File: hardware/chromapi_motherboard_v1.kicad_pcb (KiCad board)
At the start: 2 copper layers, 140 parts, among them J1 Battery Input, J10 Conn_FSR_TopLeft, J11 Conn_FSR_TopRight, J12 Conn_FSR_BotLeft, J13 Conn_FSR_BotRight, J14 RPI_Connector, J2 Power Switch, J3 USB_C_Receptacle_USB2.0_14P, J4 Conn_ST_STDC14, J5 Conn_TopLeft, J6 Conn_TopRight, J7 Conn_BotLeft, J8 Conn_BotRight, J9 Speaker connector, M1 Noctua NF-A4x10, Q1 PSMN1R5-30YL, Q2 PSMN1R5-30YL, Q3 AO4435, Q4 AO4468, U1 HY2120, U2 CN3302, U3 TPS568230, U4 LD39050PU33R, U5 74AHCT125, U6 STM32G431KBTx, U7 SN74LVC1T45DBV, U8 MAX98357A, U9 BNO055, Y1 32.768k

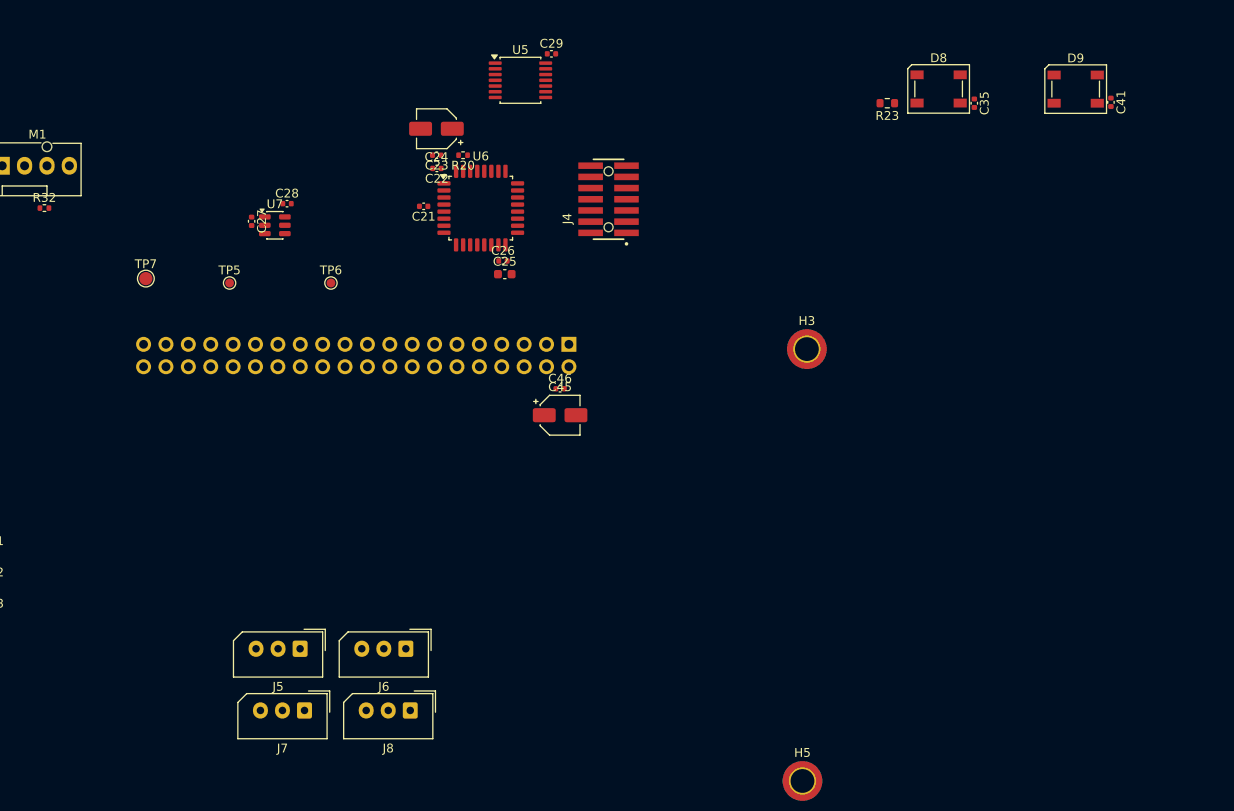
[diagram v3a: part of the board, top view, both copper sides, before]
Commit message: Adding some MPN/MPR
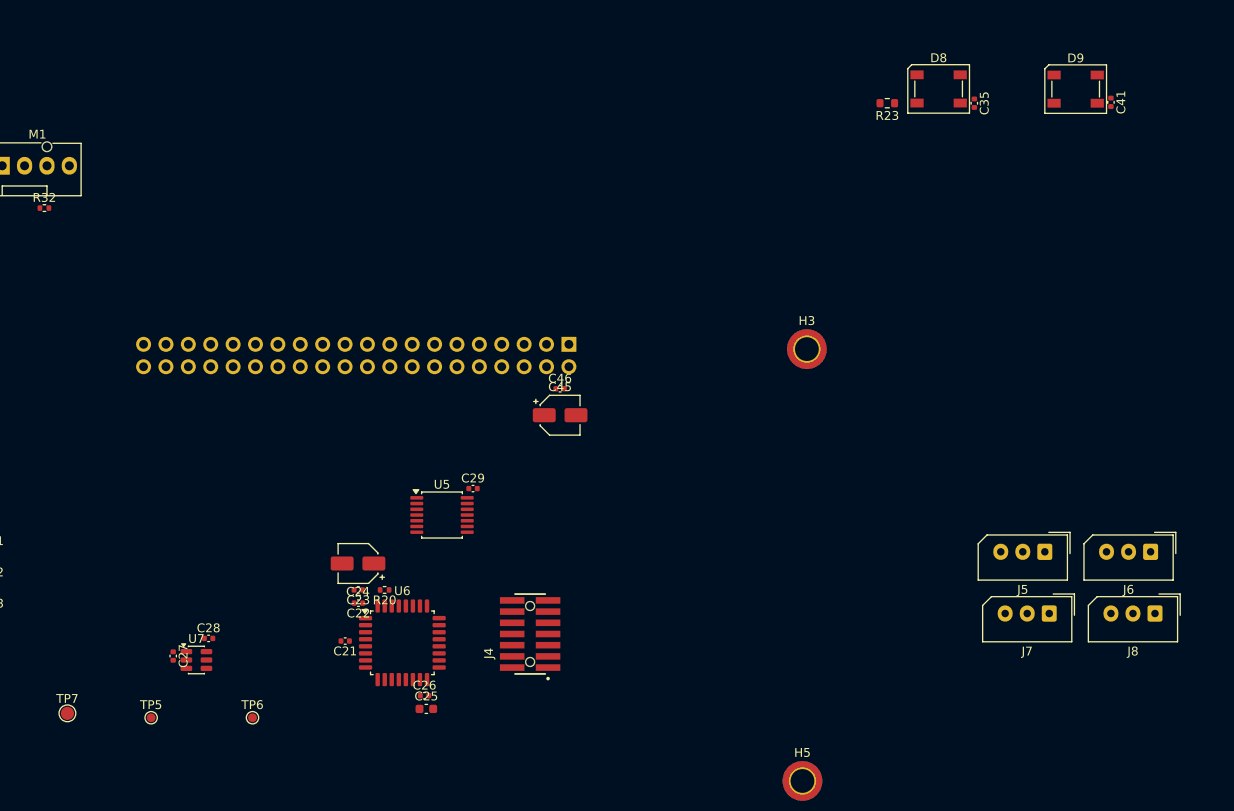
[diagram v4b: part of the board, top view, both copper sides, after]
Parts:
- moved J5 85.2 mm to (208.0, 73.5)
- moved J6 85.2 mm to (220.0, 73.5)
- moved J7 85.2 mm to (208.5, 80.5)
- moved J8 85.2 mm to (220.5, 80.5)
- moved C21 50.1 mm to (128.6, 83.6)
- moved C22 50.1 mm to (130.1, 79.3)
- moved C23 50.1 mm to (130.1, 77.8)
- moved C24 50.1 mm to (130.1, 74.8)
- moved C25 50.1 mm to (137.8, 91.3)
- moved C26 50.1 mm to (137.6, 89.8)
- moved C27 50.1 mm to (109.1, 85.3)
- moved C28 50.1 mm to (113.1, 83.3)
- moved C29 50.1 mm to (143.1, 66.3)
- moved J4 50.1 mm to (149.6, 82.8)
- moved R20 50.1 mm to (133.1, 77.8)
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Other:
- copper layers 2 -> 4
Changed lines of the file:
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@@
 	)
 	(layers
-		(0 "F.Cu" signal)
-		(2 "B.Cu" signal)
+		(0 "F.Cu" signal "F.Cu-SIGNAL")
+		(4 "In1.Cu" signal "In1.Cu-GND")
+		(6 "In2.Cu" signal "In2.Cu-PWR")
+		(2 "B.Cu" signal "B.Cu-SIGNAL")
 		(9 "F.Adhes" user "F.Adhesive")
 		(11 "B.Adhes" user "B.Adhesive")
@@
 	)
 	(setup
+		(stackup
+			(layer "F.SilkS"
+				(type "Top Silk Screen")
+			)
+			(layer "F.Paste"
+				(type "Top Solder Paste")
+			)
+			(layer "F.Mask"
+				(type "Top Solder Mask")
+				(thickness 0.01)
+			)
+			(layer "F.Cu"
+				(type "copper")
+				(thickness 0.035)
+			)
+			(layer "dielectric 1"
+				(type "prepreg")
+				(thickness 0.1)
+				(material "FR4")
+				(epsilon_r 4.5)
+				(loss_tangent 0.02)
+			)
+			(layer "In1.Cu"
+				(type "copper")
+				(thickness 0.035)
+			)
+			(layer "dielectric 2"
+				(type "core")
+				(thickness 1.24)
+				(material "FR4")
+				(epsilon_r 4.5)
+				(loss_tangent 0.02)
+			)
+			(layer "In2.Cu"
+				(type "copper")
+				(thickness 0.035)
+			)
+			(layer "dielectric 3"
+				(type "prepreg")
+				(thickness 0.1)
+				(material "FR4")
+				(epsilon_r 4.5)
+				(loss_tangent 0.02)
+			)
+			(layer "B.Cu"
+				(type "copper")
+				(thickness 0.035)
+			)
+			(layer "B.Mask"
+				(type "Bottom Solder Mask")
+				(thickness 0.01)
+			)
+			(layer "B.Paste"
+				(type "Bottom Solder Paste")
+			)
+			(layer "B.SilkS"
+				(type "Bottom Silk Screen")
+			)
+			(copper_finish "None")
+			(dielectric_constraints no)
+		)
 		(pad_to_mask_clearance 0)
+		(pad_to_paste_clearance_ratio -0.1)
 		(allow_soldermask_bridges_in_footprints no)
 		(tenting front back)
@@
 	(footprint "Capacitor_SMD:C_0402_1005Metric"
 		(layer "F.Cu")
-		(at 139 28.5 180)
+		(at 130.1 77.825 180)
 		(descr "Capacitor SMD 0402 (1005 Metric), square (rectangular) end terminal, IPC-7351 nominal, (Body size source: IPC-SM-782 page 76, https://www.pcb-3d.com/wordpress/wp-content/uploads/ipc-sm-782a_amendment_1_and_2.pdf), generated with kicad-footprint-generator")
 		(tags "capacitor")
@@
 	(footprint "Capacitor_SMD:C_0402_1005Metric"
 		(layer "F.Cu")
-		(at 146.52 40.5)
+		(at 137.62 89.825)
 		(descr "Capacitor SMD 0402 (1005 Metric), square (rectangular) end terminal, IPC-7351 nominal, (Body size source: IPC-SM-782 page 76, https://www.pcb-3d.com/wordpress/wp-content/uploads/ipc-sm-782a_amendment_1_and_2.pdf), generated with kicad-footprint-generator")
 		(tags "capacitor")
@@
 	(footprint "Package_QFP:LQFP-32_7x7mm_P0.8mm"
 		(layer "F.Cu")
-		(at 144 34.5)
+		(at 135.1 83.825)
 		(descr "LQFP, 32 Pin (https://www.nxp.com/docs/en/package-information/SOT358-1.pdf), generated with kicad-footprint-generator ipc_gullwing_generator.py")
 		(tags "LQFP QFP")
@@
 	(footprint "Capacitor_SMD:C_0402_1005Metric"
 		(layer "F.Cu")
-		(at 139.02 30 180)
+		(at 130.12 79.325 180)
 		(descr "Capacitor SMD 0402 (1005 Metric), square (rectangular) end terminal, IPC-7351 nominal, (Body size source: IPC-SM-782 page 76, https://www.pcb-3d.com/wordpress/wp-content/uploads/ipc-sm-782a_amendment_1_and_2.pdf), generated with kicad-footprint-generator")
 		(tags "capacitor")
@@
 	(footprint "Connector_Molex:Molex_SPOX_5267-03A_1x03_P2.50mm_Vertical"
 		(layer "F.Cu")
-		(at 123.5 84.5 180)
+		(at 208 73.5 180)
 		(descr "Molex SPOX Connector System, 5267-03A, 3 Pins per row (http://www.molex.com/pdm_docs/sd/022035035_sd.pdf), generated with kicad-footprint-generator")
 		(tags "connector Molex SPOX vertical")
@@
 	(footprint "Package_TO_SOT_SMD:SOT-23-6"
 		(layer "F.Cu")
-		(at 120.6375 36.45)
+		(at 111.7375 85.775)
 		(descr "SOT, 6 Pin (JEDEC MO-178 Var AB https://www.jedec.org/document_search?search_api_views_fulltext=MO-178), generated with kicad-footprint-generator ipc_gullwing_generator.py")
 		(tags "SOT TO_SOT_SMD")
@@
 	(footprint "Connector_Molex:Molex_SPOX_5267-03A_1x03_P2.50mm_Vertical"
 		(layer "F.Cu")
-		(at 136 91.5 180)
+		(at 220.5 80.5 180)
 		(descr "Molex SPOX Connector System, 5267-03A, 3 Pins per row (http://www.molex.com/pdm_docs/sd/022035035_sd.pdf), generated with kicad-footprint-generator")
 		(tags "connector Molex SPOX vertical")
@@
 	(footprint "TestPoint:TestPoint_Pad_D1.0mm"
 		(layer "F.Cu")
-		(at 115.5 43)
+		(at 106.6 92.325)
 		(descr "SMD pad as test Point, diameter 1.0mm")
 		(tags "test point SMD pad")
@@
 	(footprint "Connector_Molex:Molex_SPOX_5267-03A_1x03_P2.50mm_Vertical"
 		(layer "F.Cu")
-		(at 124 91.5 180)
+		(at 208.5 80.5 180)
 		(descr "Molex SPOX Connector System, 5267-03A, 3 Pins per row (http://www.molex.com/pdm_docs/sd/022035035_sd.pdf), generated with kicad-footprint-generator")
 		(tags "connector Molex SPOX vertical")
@@
 	(footprint "Capacitor_SMD:C_0402_1005Metric"
 		(layer "F.Cu")
-		(at 122.02 34)
+		(at 113.12 83.325)
 		(descr "Capacitor SMD 0402 (1005 Metric), square (rectangular) end terminal, IPC-7351 nominal, (Body size source: IPC-SM-782 page 76, https://www.pcb-3d.com/wordpress/wp-content/uploads/ipc-sm-782a_amendment_1_and_2.pdf), generated with kicad-footprint-generator")
 		(tags "capacitor")
@@
 	(footprint "Chromapi_FP:SAMTEC_FTSH-107-01-L-DV-K-A"
 		(layer "F.Cu")
-		(at 158.5 33.5 90)
+		(at 149.6 82.825 90)
 		(descr "translated Allegro footprint")
 		(property "Reference" "J4"
@@
 	(footprint "Capacitor_SMD:C_0402_1005Metric"
 		(layer "F.Cu")
-		(at 152.02 17)
+		(at 143.12 66.325)
 		(descr "Capacitor SMD 0402 (1005 Metric), square (rectangular) end terminal, IPC-7351 nominal, (Body size source: IPC-SM-782 page 76, https://www.pcb-3d.com/wordpress/wp-content/uploads/ipc-sm-782a_amendment_1_and_2.pdf), generated with kicad-footprint-generator")
 		(tags "capacitor")
@@
 	(footprint "Capacitor_SMD:C_0402_1005Metric"
 		(layer "F.Cu")
-		(at 137.52 34.3 180)
+		(at 128.62 83.625 180)
 		(descr "Capacitor SMD 0402 (1005 Metric), square (rectangular) end terminal, IPC-7351 nominal, (Body size source: IPC-SM-782 page 76, https://www.pcb-3d.com/wordpress/wp-content/uploads/ipc-sm-782a_amendment_1_and_2.pdf), generated with kicad-footprint-generator")
 		(tags "capacitor")
@@
 	(footprint "TestPoint:TestPoint_Pad_D1.0mm"
 		(layer "F.Cu")
-		(at 127 43)
+		(at 118.1 92.325)
 		(descr "SMD pad as test Point, diameter 1.0mm")
 		(tags "test point SMD pad")
@@
 	(footprint "Package_SO:TSSOP-14_4.4x5mm_P0.65mm"
 		(layer "F.Cu")
-		(at 148.5 20)
+		(at 139.6 69.325)
 		(descr "TSSOP, 14 Pin (JEDEC MO-153 variation AB-1, 1.00mm body thickness, https://www.jedec.org/document_search?search_api_views_fulltext=MO-153), generated with kicad-footprint-generator ipc_gullwing_generator.py")
 		(tags "TSSOP SO")
@@
 	(footprint "Capacitor_SMD:C_0603_1608Metric"
 		(layer "F.Cu")
-		(at 146.725 42)
+		(at 137.825 91.325)
 		(descr "Capacitor SMD 0603 (1608 Metric), square (rectangular) end terminal, IPC-7351 nominal, (Body size source: IPC-SM-782 page 76, https://www.pcb-3d.com/wordpress/wp-content/uploads/ipc-sm-782a_amendment_1_and_2.pdf), generated with kicad-footprint-generator")
 		(tags "capacitor")
@@
 	(footprint "Capacitor_SMD:CP_Elec_4x4.5"
 		(layer "F.Cu")
-		(at 138.97 25.5 180)
+		(at 130.07 74.825 180)
 		(descr "SMD capacitor, aluminum electrolytic, Nichicon, 4.0x4.5mm")
 		(tags "capacitor electrolytic")
@@
 	(footprint "TestPoint:TestPoint_Pad_D1.5mm"
 		(layer "F.Cu")
-		(at 106 42.5)
+		(at 97.1 91.825)
 		(descr "SMD pad as test Point, diameter 1.5mm")
 		(tags "test point SMD pad")
@@
 	(footprint "Resistor_SMD:R_0402_1005Metric"
 		(layer "F.Cu")
-		(at 141.99 28.5 180)
+		(at 133.09 77.825 180)
 		(descr "Resistor SMD 0402 (1005 Metric), square (rectangular) end terminal, IPC-7351 nominal, (Body size source: IPC-SM-782 page 72, https://www.pcb-3d.com/wordpress/wp-content/uploads/ipc-sm-782a_amendment_1_and_2.pdf), generated with kicad-footprint-generator")
 		(tags "resistor")
@@
 	(footprint "Capacitor_SMD:C_0402_1005Metric"
 		(layer "F.Cu")
-		(at 118 36 -90)
+		(at 109.1 85.325 -90)
 		(descr "Capacitor SMD 0402 (1005 Metric), square (rectangular) end terminal, IPC-7351 nominal, (Body size source: IPC-SM-782 page 76, https://www.pcb-3d.com/wordpress/wp-content/uploads/ipc-sm-782a_amendment_1_and_2.pdf), generated with kicad-footprint-generator")
 		(tags "capacitor")
@@
 	(footprint "Connector_Molex:Molex_SPOX_5267-03A_1x03_P2.50mm_Vertical"
 		(layer "F.Cu")
-		(at 135.5 84.5 180)
+		(at 220 73.5 180)
 		(descr "Molex SPOX Connector System, 5267-03A, 3 Pins per row (http://www.molex.com/pdm_docs/sd/022035035_sd.pdf), generated with kicad-footprint-generator")
 		(tags "connector Molex SPOX vertical")
@@
 		)
 		(property "Value" "RPI_Connector"
-			(at -1.27 -51.03 90)
+			(at -50.595 -59.93 90)
 			(layer "B.Fab")
 			(effects

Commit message: Updating schematic
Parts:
- added FB1: FerriteBead_Small, Inductor_SMD:L_0805_2012Metric, F.Cu at (143.1, 88.5)
- D5, D6, D7: footprint LED_SMD:LED_0402_1005Metric -> LED_SMD:LED_0603_1608Metric
- D8, D9: footprint LED_SMD:LED_SK6812_PLCC4_5.0x5.0mm_P3.2mm -> LED_SMD:LED_SK6812_EC15_1.5x1.5mm
- J9: footprint Connector_JST:JST_XH_B2B-XH-A_1x02_P2.50mm_Vertical -> Connector_JST:JST_XH_B4B-XH-A_1x04_P2.50mm_Vertical
- R17: value 3.3k -> 2.7k
- R19: value 470 -> 560
- moved J9 6.10 mm to (220.0, 106.5), turned to 0 degrees
- renumbered FB1 to FB2, FB2 to FB3
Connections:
- J9 pad 1: /Peripherals (Sensors & Audio)/SPEAKER_VO+ -> unconnected-(J9-Pin_1-Pad1)
- J9 pad 2: /Peripherals (Sensors & Audio)/SPEAKER_VO- -> /Peripherals (Sensors & Audio)/SPEAKER_VO+

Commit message: Schematic servo tranceiver correction
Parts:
- removed the R23 at (190.1, 22.6)
- added C30: 100nF, Capacitor_SMD:C_0402_1005Metric, F.Cu at (186.0, 28.0)
- added C31: 100nF, Capacitor_SMD:C_0402_1005Metric, F.Cu at (186.0, 30.0)
- added R20: 330, Resistor_SMD:R_0603_1608Metric, F.Cu at (186.6, 25.8)
- added U5: SN74AHCT1G125DBVR, Chromapi_FP:SOT95P280X145-5N, F.Cu at (183.7, 17.9)
- moved C37 23.0 mm to (220.5, 33.0)
- moved C43 13.6 mm to (226.5, 30.5)
- moved D8 1.52 mm to (195.6, 22.4)
- moved D9 1.42 mm to (210.6, 22.1)
- renumbered C30 to C32, C31 to C33, C32 to C34, C33 to C35, C34 to C36, C35 to C37, C36 to C37, C37 to C38, C38 to C39, C39 to C40, C40 to C41, C41 to C43, R20 to R21, R21 to R22, R22 to R23
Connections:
- net /Peripherals (Sensors & Audio)/LED_DATA renamed /STM32 Microcontroller Core/LED_DATA
- U6 pad 2: unconnected-(U6-PF0-Pad2) -> /Peripherals (Sensors & Audio)/FSR_TopLeft
- U6 pad 8: /Peripherals (Sensors & Audio)/FSR_TopLeft -> /STM32 Microcontroller Core/USART2_RX

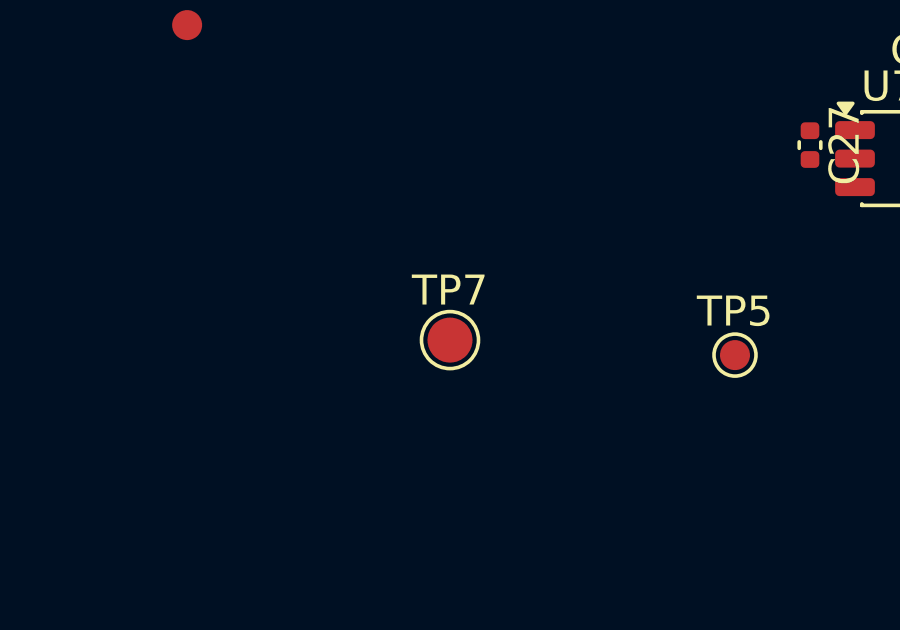
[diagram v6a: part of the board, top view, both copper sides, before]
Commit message: IMU modification and Power monitor addition
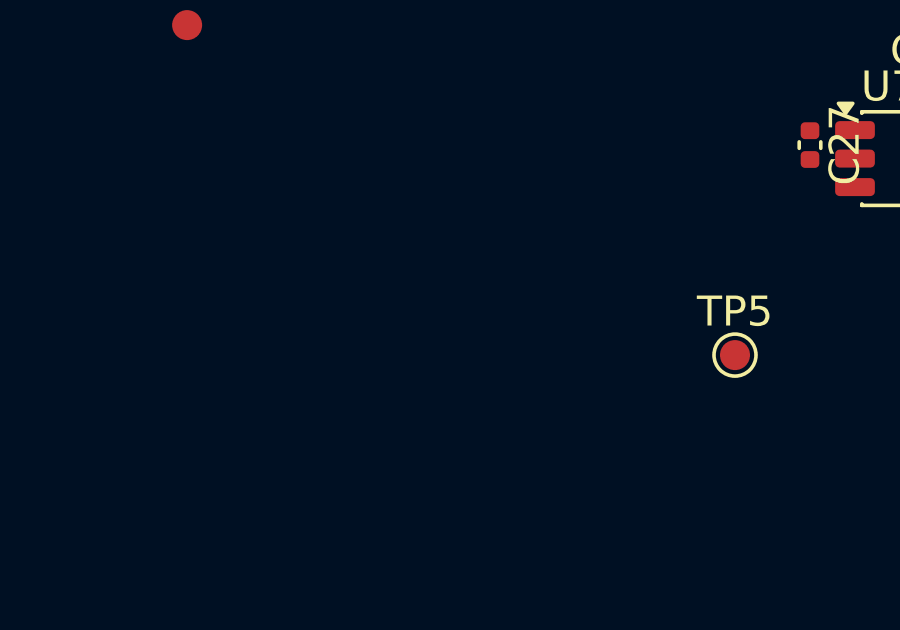
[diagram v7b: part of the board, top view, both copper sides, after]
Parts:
- removed TP7: TP_GND, TestPoint:TestPoint_Pad_D1.5mm
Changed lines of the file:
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@@
 		)
-	)
-	(footprint "TestPoint:TestPoint_Pad_D1.5mm"
-		(layer "F.Cu")
-		(at 97.1 91.825)
-		(descr "SMD pad as test Point, diameter 1.5mm")
-		(tags "test point SMD pad")
-		(property "Reference" "TP7"
-			(at 0 -1.648 0)
-			(layer "F.SilkS")
-			(effects
-				(font
-					(size 1 1)
-					(thickness 0.15)
-				)
-			)
-		)
-		(property "Value" "TP_GND"
-			(at 0 1.75 0)
-			(layer "F.Fab")
-			(effects
-				(font
-					(size 1 1)
-					(thickness 0.15)
-				)
-			)
-		)
-		(property "Datasheet" "~"
-			(at 0 0 0)
-			(unlocked yes)
-			(layer "F.Fab")
-			(hide yes)
-			(effects
-				(font
-					(size 1.27 1.27)
-					(thickness 0.15)
-				)
-			)
-		)
-		(property "Description" "test point"
-			(at 0 0 0)
-			(unlocked yes)
-			(layer "F.Fab")
-			(hide yes)
-			(effects
-				(font
-					(size 1.27 1.27)
-					(thickness 0.15)
-				)
-			)
-		)
-		(property "Sim.Device" ""
-			(at 0 0 0)
-			(unlocked yes)
-			(layer "F.Fab")
-			(hide yes)
-			(effects
-				(font
-					(size 1 1)
-					(thickness 0.15)
-				)
-			)
-		)
-		(property "Sim.Type" ""
-			(at 0 0 0)
-			(unlocked yes)
-			(layer "F.Fab")
-			(hide yes)
-			(effects
-				(font
-					(size 1 1)
-					(thickness 0.15)
-				)
-			)
-		)
-		(property ki_fp_filters "Pin* Test*")
-		(sheetname "/STM32 Microcontroller Core/")
-		(sheetfile "stm32_mcu_core.kicad_sch")
-		(attr exclude_from_pos_files)
-		(fp_circle
-			(center 0 0)
-			(end 0 0.95)
-			(stroke
-				(width 0.12)
-				(type solid)
-			)
-			(fill no)
-			(layer "F.SilkS")
-		)
-		(fp_circle
-			(center 0 0)
-			(end 1.25 0)
-			(stroke
-				(width 0.05)
-				(type solid)
-			)
-			(fill no)
-			(layer "F.CrtYd")
-		)
-		(fp_text user "${REFERENCE}"
-			(at 0 -1.65 0)
-			(layer "F.Fab")
-			(effects
-				(font
-					(size 1 1)
-					(thickness 0.15)
-				)
-			)
-		)
-		(pad "1" smd circle
-			(at 0 0)
-			(size 1.5 1.5)
-			(layers "F.Cu" "F.Mask")
-			(net 4 "GND")
-			(pinfunction "1")
-			(pintype "passive")
-		)
-		(embedded_fonts no)
 	)
 	(footprint "MountingHole:MountingHole_2.7mm_M2.5_ISO14580_Pad_TopBottom"
